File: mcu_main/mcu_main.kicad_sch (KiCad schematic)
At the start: 23 parts, among them SW1 SW_Push_Dual, SW2 SW_Push_Dual, U1 ESP32-S3-WROOM-1, U3 SGM2212-3.3, U5 SGM2212-2.8

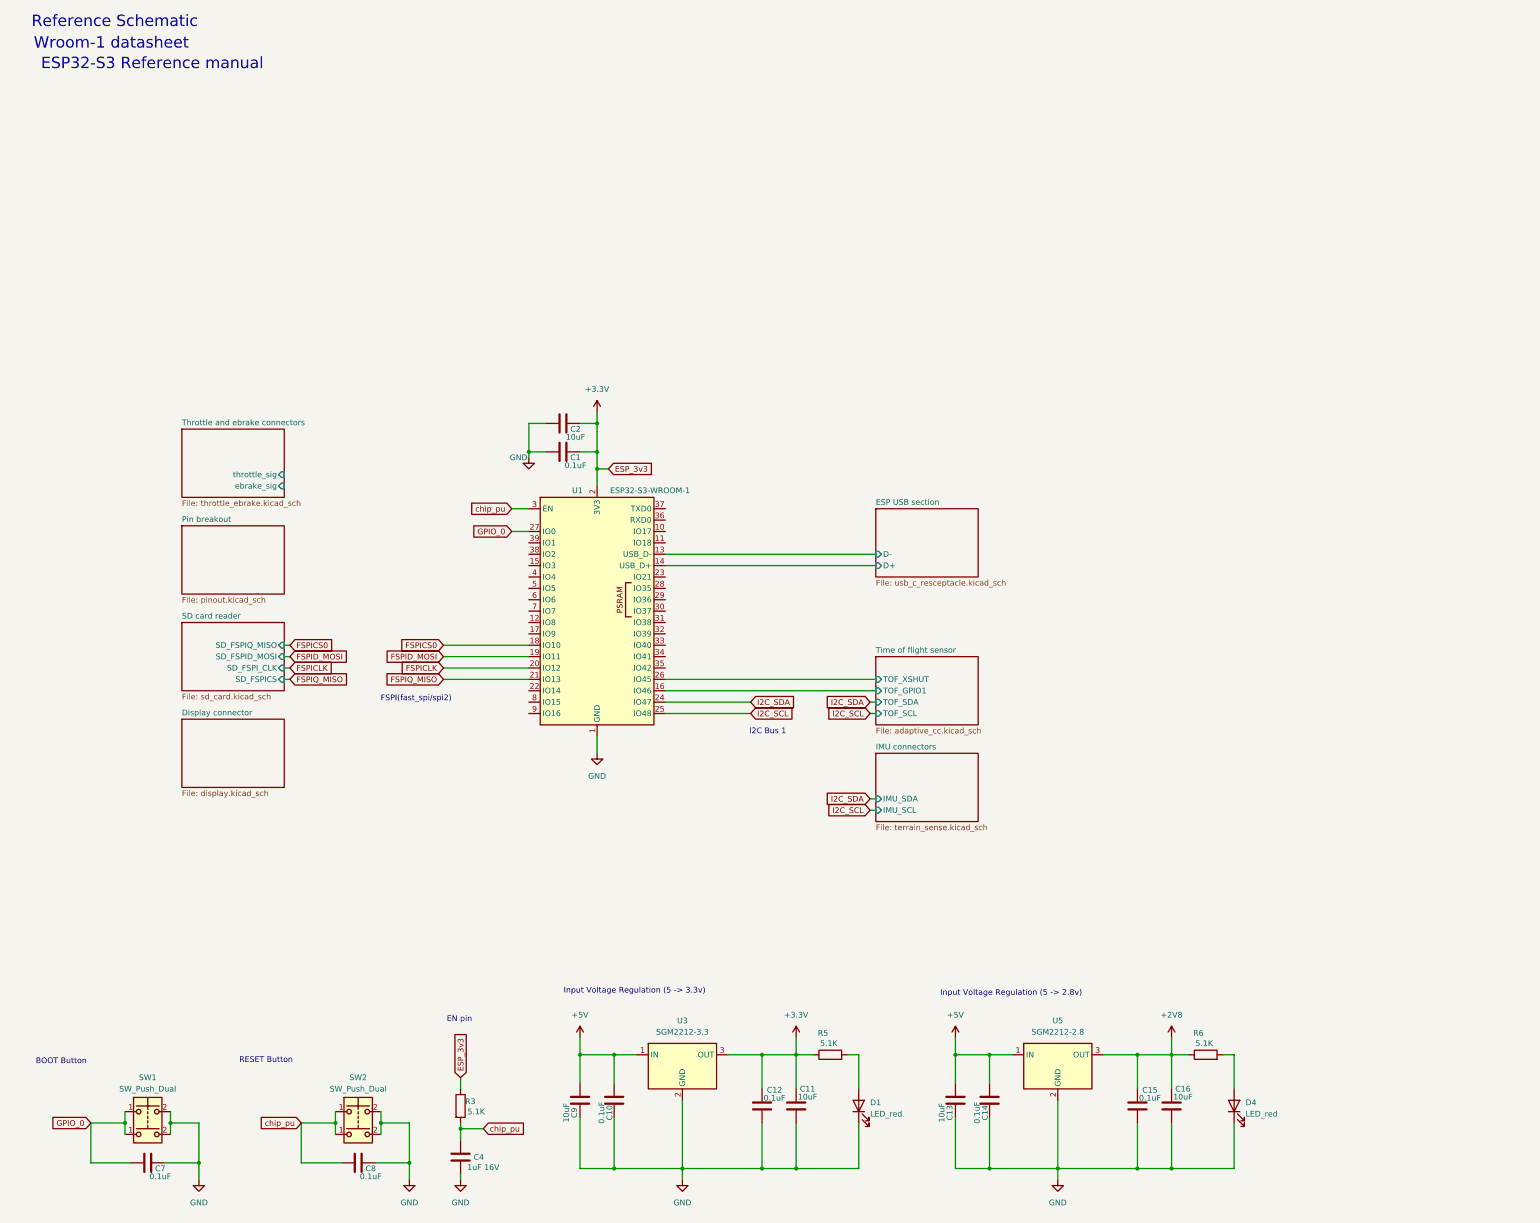
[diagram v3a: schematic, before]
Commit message: added throttle and ebrake connectors
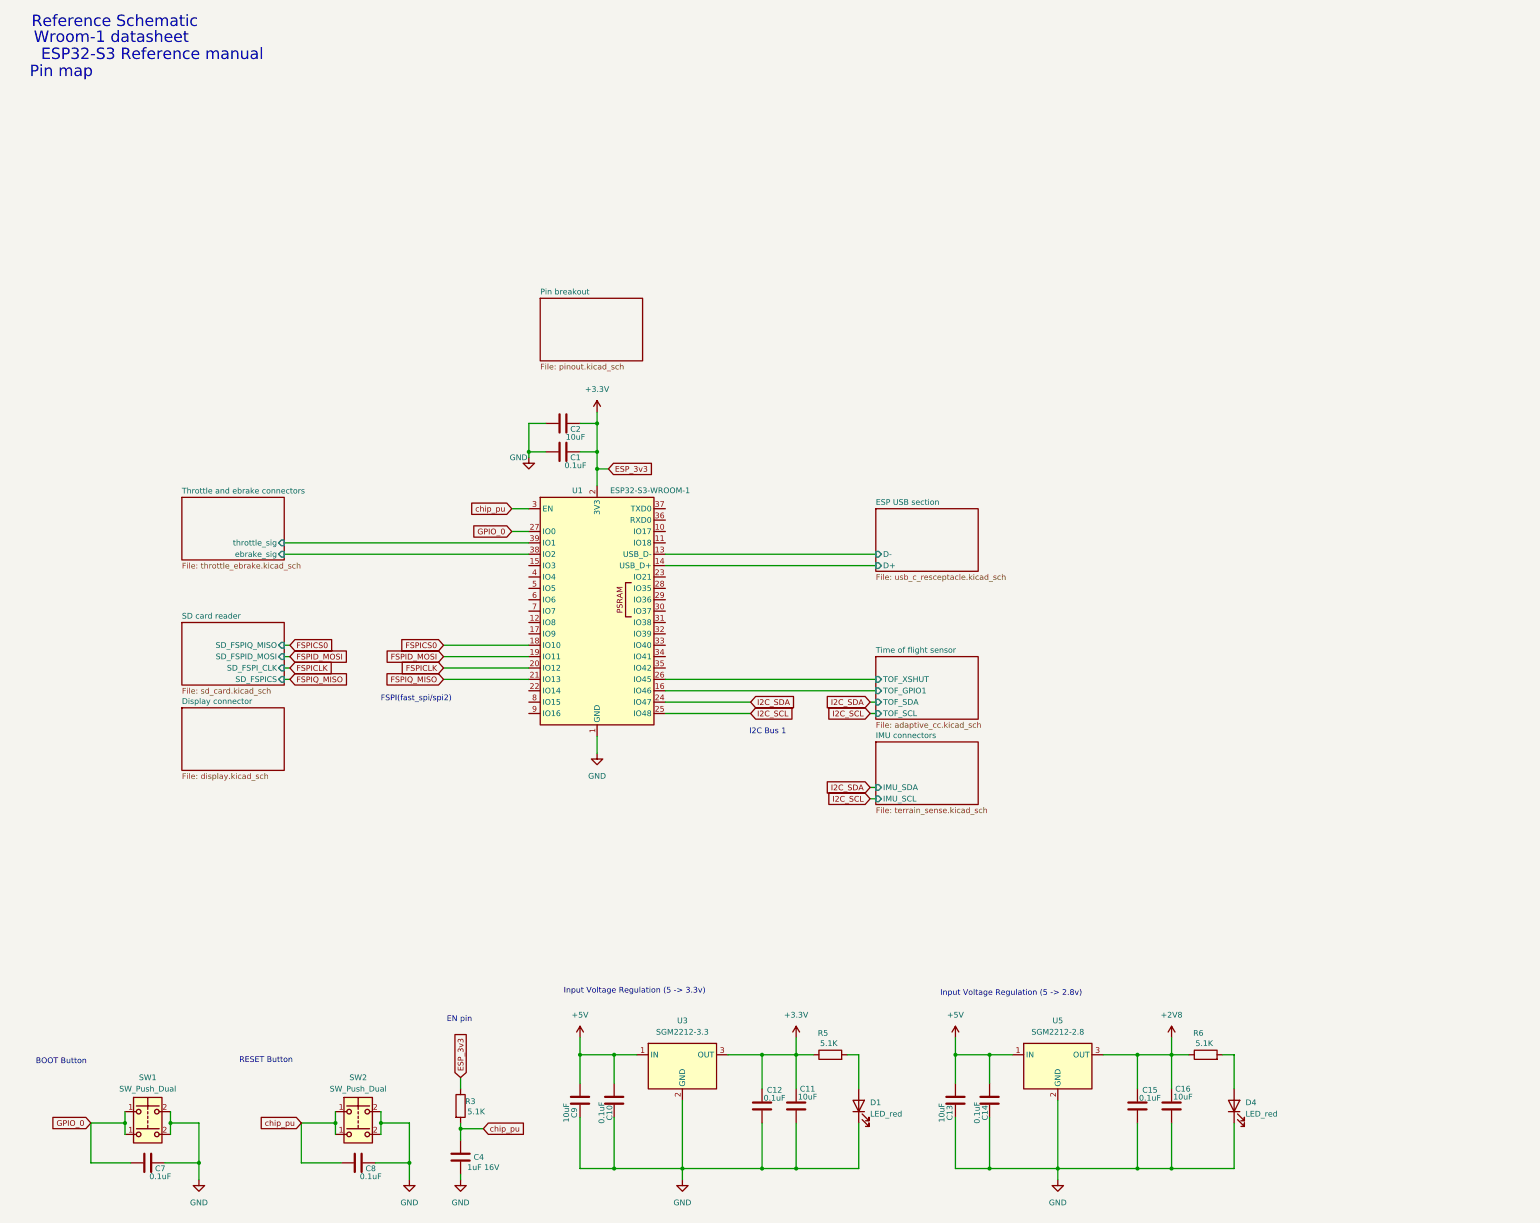
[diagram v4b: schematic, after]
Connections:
- net Throttle and ebrake connectors/ebrake_sig: now also U1.38 (IO2)
- net Throttle and ebrake connectors/throttle_sig: now also U1.39 (IO1)
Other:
- note added: "Pin map"
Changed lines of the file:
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@@
 	(text "Wroom-1 datasheet"
 		(exclude_from_sim no)
-		(at 32.512 20.574 0)
+		(at 32.512 19.304 0)
 		(effects
 			(font
@@
 		)
 	)
+	(text "Pin map"
+		(exclude_from_sim no)
+		(at 21.336 26.924 0)
+		(effects
+			(font
+				(size 2.54 2.54)
+			)
+			(href "https://randomnerdtutorials.com/esp32-s3-devkitc-pinout-guide/")
+		)
+	)
 	(text "RESET Button"
 		(exclude_from_sim no)
@@
 	(text "ESP32-S3 Reference manual"
 		(exclude_from_sim no)
-		(at 41.656 25.146 0)
+		(at 41.656 23.114 0)
 		(effects
 			(font
@@
 	(wire
 		(pts
+			(xy 71.12 134.62) (xy 125.73 134.62)
+		)
+		(stroke
+			(width 0)
+			(type default)
+		)
+	)
+	(wire
+		(pts
 			(xy 44.45 270.51) (xy 52.07 270.51)
 		)
@@
 	(wire
 		(pts
-			(xy 201.93 191.77) (xy 203.2 191.77)
+			(xy 201.93 189.23) (xy 203.2 189.23)
 		)
 		(stroke
@@
 	(wire
 		(pts
+			(xy 71.12 132.08) (xy 125.73 132.08)
+		)
+		(stroke
+			(width 0)
+			(type default)
+		)
+	)
+	(wire
+		(pts
 			(xy 140.97 179.07) (xy 140.97 175.26)
 		)
@@
 	(wire
 		(pts
-			(xy 201.93 189.23) (xy 203.2 189.23)
+			(xy 201.93 186.69) (xy 203.2 186.69)
 		)
 		(stroke
@@
 	(global_label "I2C_SCL"
 		(shape input)
-		(at 201.93 191.77 180)
+		(at 201.93 189.23 180)
 		(fields_autoplaced yes)
 		(effects
@@
 		)
 		(property "Intersheetrefs" "${INTERSHEET_REFS}"
-			(at 191.3853 191.77 0)
+			(at 191.3853 189.23 0)
 			(effects
 				(font
@@
 	(global_label "I2C_SDA"
 		(shape input)
-		(at 201.93 189.23 180)
+		(at 201.93 186.69 180)
 		(fields_autoplaced yes)
 		(effects
@@
 		)
 		(property "Intersheetrefs" "${INTERSHEET_REFS}"
-			(at 191.3248 189.23 0)
+			(at 191.3248 186.69 0)
 			(effects
 				(font
@@
 	)
 	(sheet
-		(at 48.26 171.45)
-		(size 22.86 15.24)
+		(at 48.26 168.91)
+		(size 22.86 13.97)
 		(exclude_from_sim no)
 		(in_bom yes)
@@
 		)
 		(property "Sheetname" "Display connector"
-			(at 48.26 170.7384 0)
+			(at 48.26 168.1984 0)
 			(effects
 				(font
@@
 		)
 		(property "Sheetfile" "display.kicad_sch"
-			(at 48.26 187.2746 0)
+			(at 48.26 183.4646 0)
 			(effects
 				(font
@@
 	(sheet
 		(at 203.2 124.46)
-		(size 22.86 15.24)
+		(size 22.86 13.97)
 		(exclude_from_sim no)
 		(in_bom yes)
@@
 		)
 		(property "Sheetfile" "usb_c_resceptacle.kicad_sch"
-			(at 203.2 140.2846 0)
+			(at 203.2 139.0146 0)
 			(effects
 				(font
@@
 	)
 	(sheet
-		(at 48.26 106.68)
-		(size 22.86 15.24)
+		(at 48.26 121.92)
+		(size 22.86 13.97)
 		(exclude_from_sim no)
 		(in_bom yes)
@@
 		)
 		(property "Sheetname" "Throttle and ebrake connectors"
-			(at 48.26 105.9684 0)
+			(at 48.26 121.2084 0)
 			(effects
 				(font
@@
 		)
 		(property "Sheetfile" "throttle_ebrake.kicad_sch"
-			(at 48.26 122.5046 0)
+			(at 48.26 136.4746 0)
 			(effects
 				(font
@@
 		)
 		(pin "ebrake_sig" input
-			(at 71.12 119.38 0)
+			(at 71.12 134.62 0)
 			(effects
 				(font
@@
 		)
 		(pin "throttle_sig" input
-			(at 71.12 116.84 0)
+			(at 71.12 132.08 0)
 			(effects
 				(font
@@
 	(sheet
 		(at 48.26 149.86)
-		(size 22.86 15.2399)
+		(size 22.86 13.97)
 		(exclude_from_sim no)
 		(in_bom yes)
@@
 		)
 		(property "Sheetfile" "sd_card.kicad_sch"
-			(at 48.26 165.6845 0)
+			(at 48.26 164.4146 0)
 			(effects
 				(font
@@
 	)
 	(sheet
-		(at 48.26 128.27)
-		(size 22.86 15.24)
+		(at 128.27 77.47)
+		(size 22.86 13.97)
 		(exclude_from_sim no)
 		(in_bom yes)
@@
 		)
 		(property "Sheetname" "Pin breakout"
-			(at 48.26 127.5584 0)
+			(at 128.27 76.7584 0)
 			(effects
 				(font
@@
 		)
 		(property "Sheetfile" "pinout.kicad_sch"
-			(at 48.26 144.0946 0)
+			(at 128.27 92.0246 0)
 			(effects
 				(font
@@
 	(sheet
 		(at 203.2 157.48)
-		(size 22.86 15.24)
+		(size 22.86 13.97)
 		(exclude_from_sim no)
 		(in_bom yes)
@@
 		)
 		(property "Sheetfile" "adaptive_cc.kicad_sch"
-			(at 203.2 173.3046 0)
+			(at 203.2 172.0346 0)
 			(effects
 				(font
@@
 	)
 	(sheet
-		(at 203.2 179.07)
-		(size 22.86 15.24)
+		(at 203.2 176.53)
+		(size 22.86 13.97)
 		(exclude_from_sim no)
 		(in_bom yes)
@@
 		)
 		(property "Sheetname" "IMU connectors"
-			(at 203.2 178.3584 0)
+			(at 203.2 175.8184 0)
 			(effects
 				(font
@@
 		)
 		(property "Sheetfile" "terrain_sense.kicad_sch"
-			(at 203.2 194.8946 0)
+			(at 203.2 191.0846 0)
 			(effects
 				(font
@@
 		)
 		(pin "IMU_SCL" input
-			(at 203.2 191.77 180)
+			(at 203.2 189.23 180)
 			(effects
 				(font
@@
 		)
 		(pin "IMU_SDA" input
-			(at 203.2 189.23 180)
+			(at 203.2 186.69 180)
 			(effects
 				(font

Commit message: pas sensors
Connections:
- net PAS connector/speed_sig_1: now reaches U1.4 (IO4)
- net PAS connector/speed_sig_2: now reaches U1.5 (IO5)
- net PAS connector/torque_sig: now reaches U1.6 (IO6)
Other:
- added sheet PAS connector (pas_sensor.kicad_sch)
- moved on the sheet: C10, C11, C12, C13, C14, C15, C16, C4, C7, C8, C9, D1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
